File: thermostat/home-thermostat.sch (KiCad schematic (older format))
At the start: 49 parts, among them J1 Amphenol_132289 SMA, J4 Conn_ARM_JTAG_SWD_10, J7 UART, U1 MKW41Z512VHT, U10 SN74LVC2T45DCUR, U9 SN74LVC2T45DCUR, Y1 32MHz 10PPM SMT 2.0x1.6mm 10PF, Y2 32.768KHz 20PPM 3.2x1.5mm 7PF

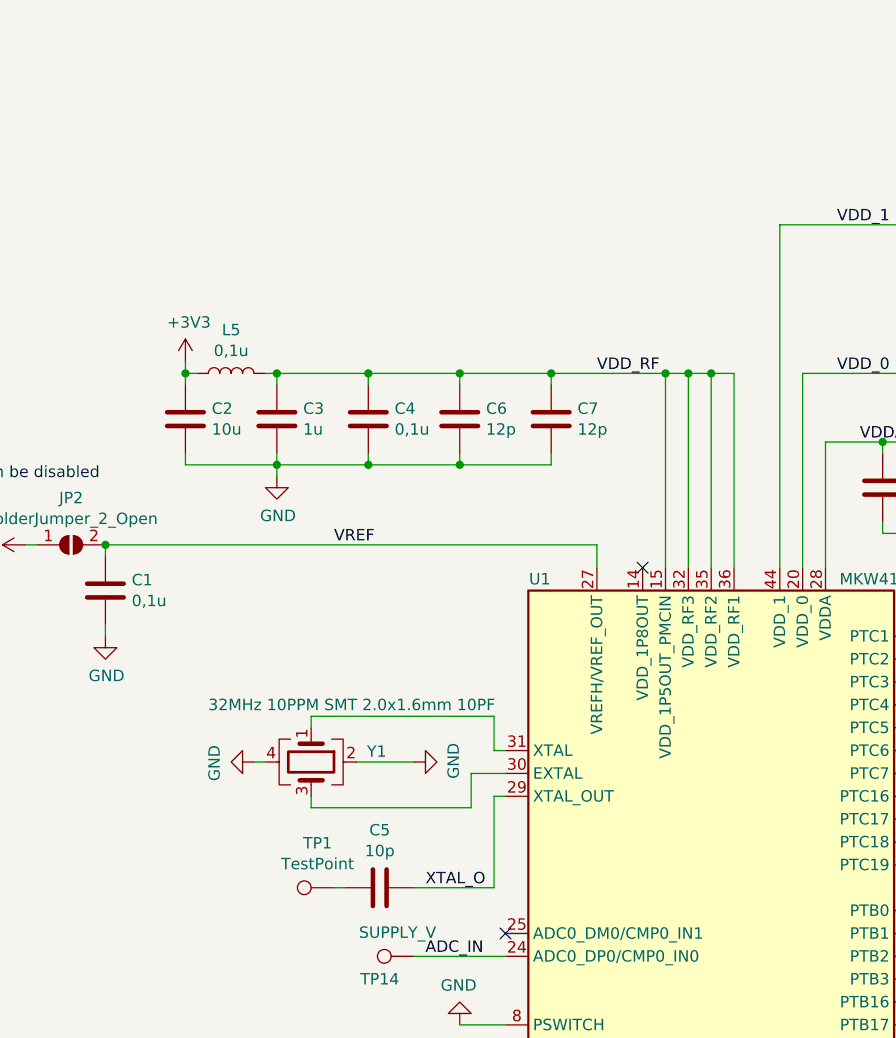
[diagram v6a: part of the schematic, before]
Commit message: Modivied DRC constraints according to specs of PCB_POOL, finished layouting signal lines, only power is left.
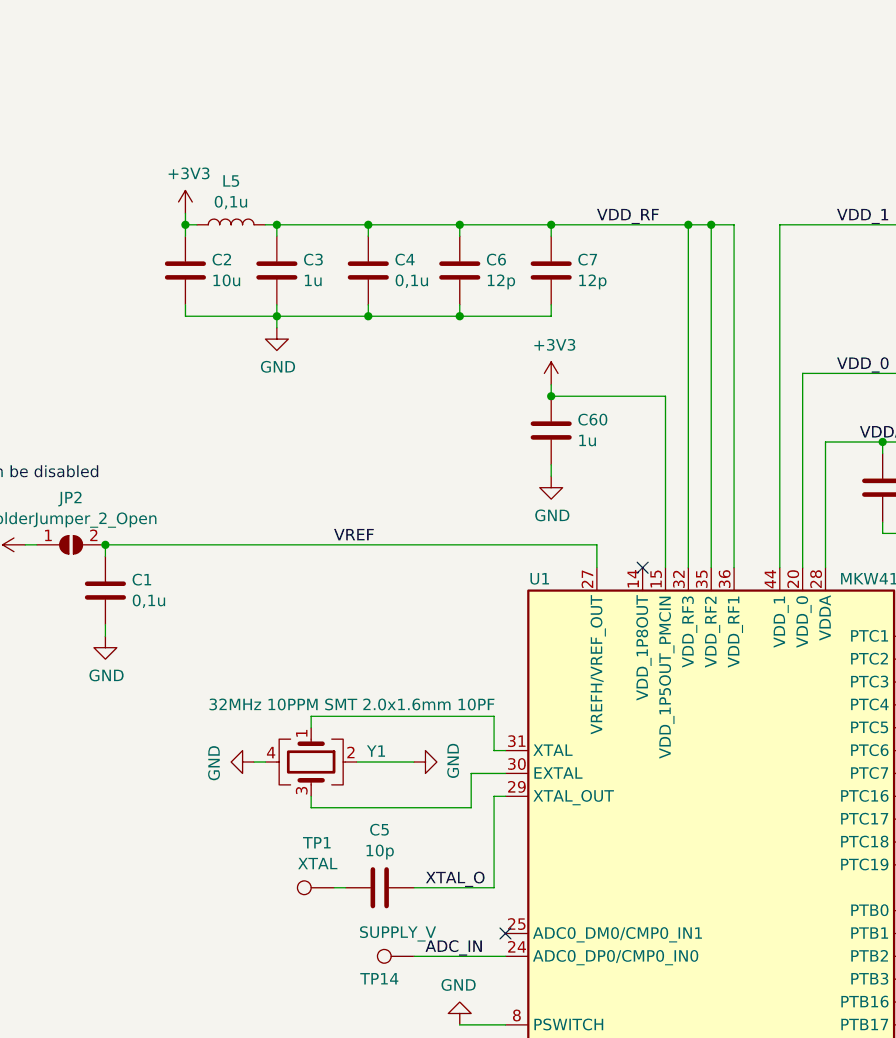
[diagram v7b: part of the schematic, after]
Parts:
- added C60: 1u, Capacitor_SMD:C_0402_1005Metric, symbol Device:C
- TP1: value TestPoint -> XTAL
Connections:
- net +3V3: now also U1.15 (VDD_1P5OUT_PMCIN), C60.1
- net GND: now also C60.2
- net VDD_RF: no longer U1.15 (VDD_1P5OUT_PMCIN)
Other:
- moved on the sheet: C2, C3, C4, C6, C7, L5
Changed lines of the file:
@@
 L power:+3V3 #PWR?
 U 1 1 5F34B539
-P 4450 1350
+P 4450 700
 AR Path="/5E8AC4D3/5F34B539" Ref="#PWR?"  Part="1"
 AR Path="/5F34B539" Ref="#PWR03"  Part="1"
-F 0 "#PWR03" H 4450 1200 50  0001 C CNN
-F 1 "+3V3" H 4465 1523 50  0000 C CNN
-F 2 "" H 4450 1350 50  0001 C CNN
-F 3 "" H 4450 1350 50  0001 C CNN
-	1    4450 1350
+F 0 "#PWR03" H 4450 550 50  0001 C CNN
+F 1 "+3V3" H 4465 873 50  0000 C CNN
+F 2 "" H 4450 700 50  0001 C CNN
+F 3 "" H 4450 700 50  0001 C CNN
+	1    4450 700
 	1    0    0    -1
 $EndComp
@@
 L Device:C C7
 U 1 1 5F34BEFE
-P 6050 1600
-F 0 "C7" H 6165 1646 50  0000 L CNN
-F 1 "12p" H 6165 1555 50  0000 L CNN
-F 2 "Capacitor_SMD:C_0402_1005Metric" H 6088 1450 50  0001 C CNN
-F 3 "~" H 6050 1600 50  0001 C CNN
-	1    6050 1600
+P 6050 950
+F 0 "C7" H 6165 996 50  0000 L CNN
+F 1 "12p" H 6165 905 50  0000 L CNN
+F 2 "Capacitor_SMD:C_0402_1005Metric" H 6088 800 50  0001 C CNN
+F 3 "~" H 6050 950 50  0001 C CNN
+	1    6050 950
 	1    0    0    -1
 $EndComp
@@
 L Device:C C6
 U 1 1 5F34C514
-P 5650 1600
-F 0 "C6" H 5765 1646 50  0000 L CNN
-F 1 "12p" H 5765 1555 50  0000 L CNN
-F 2 "Capacitor_SMD:C_0402_1005Metric" H 5688 1450 50  0001 C CNN
-F 3 "~" H 5650 1600 50  0001 C CNN
-	1    5650 1600
+P 5650 950
+F 0 "C6" H 5765 996 50  0000 L CNN
+F 1 "12p" H 5765 905 50  0000 L CNN
+F 2 "Capacitor_SMD:C_0402_1005Metric" H 5688 800 50  0001 C CNN
+F 3 "~" H 5650 950 50  0001 C CNN
+	1    5650 950
 	1    0    0    -1
 $EndComp
@@
 L Device:C C4
 U 1 1 5F34C6C2
-P 5250 1600
-F 0 "C4" H 5365 1646 50  0000 L CNN
-F 1 "0,1u" H 5365 1555 50  0000 L CNN
-F 2 "Capacitor_SMD:C_0402_1005Metric" H 5288 1450 50  0001 C CNN
-F 3 "~" H 5250 1600 50  0001 C CNN
-	1    5250 1600
+P 5250 950
+F 0 "C4" H 5365 996 50  0000 L CNN
+F 1 "0,1u" H 5365 905 50  0000 L CNN
+F 2 "Capacitor_SMD:C_0402_1005Metric" H 5288 800 50  0001 C CNN
+F 3 "~" H 5250 950 50  0001 C CNN
+	1    5250 950
 	1    0    0    -1
 $EndComp
@@
 L Device:C C3
 U 1 1 5F34C88C
-P 4850 1600
-F 0 "C3" H 4965 1646 50  0000 L CNN
-F 1 "1u" H 4965 1555 50  0000 L CNN
-F 2 "Capacitor_SMD:C_0402_1005Metric" H 4888 1450 50  0001 C CNN
-F 3 "~" H 4850 1600 50  0001 C CNN
-	1    4850 1600
+P 4850 950
+F 0 "C3" H 4965 996 50  0000 L CNN
+F 1 "1u" H 4965 905 50  0000 L CNN
+F 2 "Capacitor_SMD:C_0402_1005Metric" H 4888 800 50  0001 C CNN
+F 3 "~" H 4850 950 50  0001 C CNN
+	1    4850 950
 	1    0    0    -1
 $EndComp
@@
 L Device:C C2
 U 1 1 5F364B46
-P 4450 1600
-F 0 "C2" H 4335 1554 50  0000 R CNN
-F 1 "10u" H 4335 1645 50  0000 R CNN
-F 2 "Capacitor_SMD:C_0603_1608Metric" H 4488 1450 50  0001 C CNN
-F 3 "~" H 4450 1600 50  0001 C CNN
-	1    4450 1600
+P 4450 950
+F 0 "C2" H 4335 904 50  0000 R CNN
+F 1 "10u" H 4335 995 50  0000 R CNN
+F 2 "Capacitor_SMD:C_0603_1608Metric" H 4488 800 50  0001 C CNN
+F 3 "~" H 4450 950 50  0001 C CNN
+	1    4450 950
 	-1   0    0    1
 $EndComp
@@
 $EndComp
 Wire Wire Line
-	4850 1400 5250 1400
-Wire Wire Line
-	4850 1450 4850 1400
-Wire Wire Line
-	5250 1450 5250 1400
-Connection ~ 5250 1400
-Wire Wire Line
-	5250 1400 5650 1400
-Wire Wire Line
-	5650 1450 5650 1400
-Connection ~ 5650 1400
-Wire Wire Line
-	5650 1400 6050 1400
-Wire Wire Line
-	6050 1450 6050 1400
-Connection ~ 6050 1400
+	4850 750  5250 750
+Wire Wire Line
+	4850 800  4850 750
+Wire Wire Line
+	5250 800  5250 750
+Connection ~ 5250 750
+Wire Wire Line
+	5250 750  5650 750
+Wire Wire Line
+	5650 800  5650 750
+Connection ~ 5650 750
+Wire Wire Line
+	5650 750  6050 750
+Wire Wire Line
+	6050 800  6050 750
+Connection ~ 6050 750
 NoConn ~ 5850 4950
 NoConn ~ 5850 5050
@@
 L power:GND #PWR?
 U 1 1 5F3A2757
-P 4850 1850
+P 4850 1200
 AR Path="/5E8AC4D3/5F3A2757" Ref="#PWR?"  Part="1"
 AR Path="/5F3A2757" Ref="#PWR05"  Part="1"
-F 0 "#PWR05" H 4850 1600 50  0001 C CNN
-F 1 "GND" H 4855 1677 50  0000 C CNN
-F 2 "" H 4850 1850 50  0001 C CNN
-F 3 "" H 4850 1850 50  0001 C CNN
-	1    4850 1850
-	1    0    0    -1
-$EndComp
-Wire Wire Line
-	4850 1850 4850 1800
-Wire Wire Line
-	6050 1750 6050 1800
-Wire Wire Line
-	6050 1800 5650 1800
-Connection ~ 4850 1800
-Wire Wire Line
-	4850 1800 4850 1750
-Wire Wire Line
-	5250 1750 5250 1800
-Connection ~ 5250 1800
-Wire Wire Line
-	5250 1800 4850 1800
-Wire Wire Line
-	5650 1750 5650 1800
-Connection ~ 5650 1800
-Wire Wire Line
-	5650 1800 5250 1800
+F 0 "#PWR05" H 4850 950 50  0001 C CNN
+F 1 "GND" H 4855 1027 50  0000 C CNN
+F 2 "" H 4850 1200 50  0001 C CNN
+F 3 "" H 4850 1200 50  0001 C CNN
+	1    4850 1200
+	1    0    0    -1
+$EndComp
+Wire Wire Line
+	4850 1200 4850 1150
+Wire Wire Line
+	6050 1100 6050 1150
+Wire Wire Line
+	6050 1150 5650 1150
+Connection ~ 4850 1150
+Wire Wire Line
+	4850 1150 4850 1100
+Wire Wire Line
+	5250 1100 5250 1150
+Connection ~ 5250 1150
+Wire Wire Line
+	5250 1150 4850 1150
+Wire Wire Line
+	5650 1100 5650 1150
+Connection ~ 5650 1150
+Wire Wire Line
+	5650 1150 5250 1150
 $Comp
 L power:GND #PWR?
@@
 P 5100 3650
 F 0 "TP1" V 5295 3722 50  0000 C CNN
-F 1 "TestPoint" V 5204 3722 50  0000 C CNN
+F 1 "XTAL" V 5204 3722 50  0000 C CNN
 F 2 "TestPoint:TestPoint_Pad_D1.0mm" H 5300 3650 50  0001 C CNN
 F 3 "~" H 5300 3650 50  0001 C CNN
@@
 	7250 1700 7250 2250
 Wire Wire Line
-	4850 1800 4450 1800
-Wire Wire Line
-	4450 1800 4450 1750
-Wire Wire Line
-	6550 1400 6650 1400
-Connection ~ 6550 1400
-Wire Wire Line
-	6650 1400 6750 1400
-Connection ~ 6650 1400
-Wire Wire Line
-	6750 1400 6850 1400
-Connection ~ 6750 1400
-Wire Wire Line
-	6550 1400 6550 2250
-Wire Wire Line
-	6650 1400 6650 2250
-Wire Wire Line
-	6750 1400 6750 2250
-Wire Wire Line
-	6850 1400 6850 2250
+	4850 1150 4450 1150
+Wire Wire Line
+	4450 1150 4450 1100
+Wire Wire Line
+	6650 750  6750 750
+Connection ~ 6650 750
+Wire Wire Line
+	6750 750  6850 750
+Connection ~ 6750 750
 Wire Wire Line
 	6250 2150 6250 2250
@@
 	8450 5450 8850 5450
 Wire Wire Line
-	4450 1350 4450 1400
-Wire Wire Line
-	4500 1400 4450 1400
-Connection ~ 4450 1400
-Wire Wire Line
-	4450 1400 4450 1450
-Wire Wire Line
-	4800 1400 4850 1400
-Connection ~ 4850 1400
+	4450 700  4450 750
+Wire Wire Line
+	4500 750  4450 750
+Connection ~ 4450 750
+Wire Wire Line
+	4450 750  4450 800
+Wire Wire Line
+	4800 750  4850 750
+Connection ~ 4850 750
 $Comp
 L Device:L L5
 U 1 1 5F6F46C0
-P 4650 1400
-F 0 "L5" V 4840 1400 50  0000 C CNN
-F 1 "0,1u" V 4749 1400 50  0000 C CNN
-F 2 "Inductor_SMD:L_0402_1005Metric" H 4650 1400 50  0001 C CNN
-F 3 "~" H 4650 1400 50  0001 C CNN
-	1    4650 1400
+P 4650 750
+F 0 "L5" V 4840 750 50  0000 C CNN
+F 1 "0,1u" V 4749 750 50  0000 C CNN
+F 2 "Inductor_SMD:L_0402_1005Metric" H 4650 750 50  0001 C CNN
+F 3 "~" H 4650 750 50  0001 C CNN
+	1    4650 750
 	0    -1   -1   0
 $EndComp
@@
 NoConn ~ 7650 -500
 NoConn ~ 8150 -500
-Wire Wire Line
-	6050 1400 6550 1400
 NoConn ~ 6450 2250
 $Comp
@@
 Text Label 5100 2150 0    50   ~ 0
 VREF
-Text Label 6250 1400 0    50   ~ 0
+Text Label 6250 750  0    50   ~ 0
 VDD_RF
 Text Label 7400 1700 0    50   ~ 0
@@
 Wire Wire Line
 	8200 2950 7650 2950
+Wire Wire Line
+	6650 750  6650 2250
+Wire Wire Line
+	6750 750  6750 2250
+Wire Wire Line
+	6850 750  6850 2250
+Wire Wire Line
+	6050 750  6650 750
+$Comp
+L Device:C C60
+U 1 1 5F82EA7F
+P 6050 1650
+F 0 "C60" H 6165 1696 50  0000 L CNN
+F 1 "1u" H 6165 1605 50  0000 L CNN
+F 2 "Capacitor_SMD:C_0402_1005Metric" H 6088 1500 50  0001 C CNN
+F 3 "~" H 6050 1650 50  0001 C CNN
+	1    6050 1650
+	1    0    0    -1
+$EndComp
+$Comp
+L power:+3V3 #PWR?
+U 1 1 5F82F6E7
+P 6050 1450
+AR Path="/5E8AC4D3/5F82F6E7" Ref="#PWR?"  Part="1"
+AR Path="/5F82F6E7" Ref="#PWR065"  Part="1"
+F 0 "#PWR065" H 6050 1300 50  0001 C CNN
+F 1 "+3V3" H 6065 1623 50  0000 C CNN
+F 2 "" H 6050 1450 50  0001 C CNN
+F 3 "" H 6050 1450 50  0001 C CNN
+	1    6050 1450
+	1    0    0    -1
+$EndComp
+$Comp
+L power:GND #PWR?
+U 1 1 5F82FCF7
+P 6050 1850
+AR Path="/5E8AC4D3/5F82FCF7" Ref="#PWR?"  Part="1"
+AR Path="/5F82FCF7" Ref="#PWR066"  Part="1"
+F 0 "#PWR066" H 6050 1600 50  0001 C CNN
+F 1 "GND" H 6055 1677 50  0000 C CNN
+F 2 "" H 6050 1850 50  0001 C CNN
+F 3 "" H 6050 1850 50  0001 C CNN
+	1    6050 1850
+	1    0    0    -1
+$EndComp
+Wire Wire Line
+	6050 1850 6050 1800
+Wire Wire Line
+	6050 1450 6050 1500
+Wire Wire Line
+	6050 1500 6550 1500
+Wire Wire Line
+	6550 1500 6550 2250
+Connection ~ 6050 1500
 $EndSCHEMATC

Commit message: Changed footprint of MKW41Z to one with individual center GND pads and no thermal vias so that I am able to set own via sizes for the thermals.
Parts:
- U1: footprint Package_DFN_QFN:NXP_LQFN-48-1EP_7x7mm_P0.5mm_EP3.5x3.5mm_16xMask0.45x0.45_ThermalVias -> Package_DFN_QFN:NXP_LQFN-48-1EP_7x7mm_P0.5mm_EP3.5x3.5mm_16xMask0.45x0.45
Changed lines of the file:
@@
 F 0 "U1" H 6000 5800 50  0000 C CNN
 F 1 "MKW41Z512VHT" H 7600 5800 50  0000 C CNN
-F 2 "Package_DFN_QFN:NXP_LQFN-48-1EP_7x7mm_P0.5mm_EP3.5x3.5mm_16xMask0.45x0.45_ThermalVias" H 6700 4050 50  0001 C CNN
+F 2 "Package_DFN_QFN:NXP_LQFN-48-1EP_7x7mm_P0.5mm_EP3.5x3.5mm_16xMask0.45x0.45" H 6700 4050 50  0001 C CNN
 F 3 "https://www.nxp.com/docs/en/data-sheet/MKW41Z512.pdf" H 6750 3950 50  0001 C CNN
 	1    6750 4050
